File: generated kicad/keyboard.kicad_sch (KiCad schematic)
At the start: 190 parts

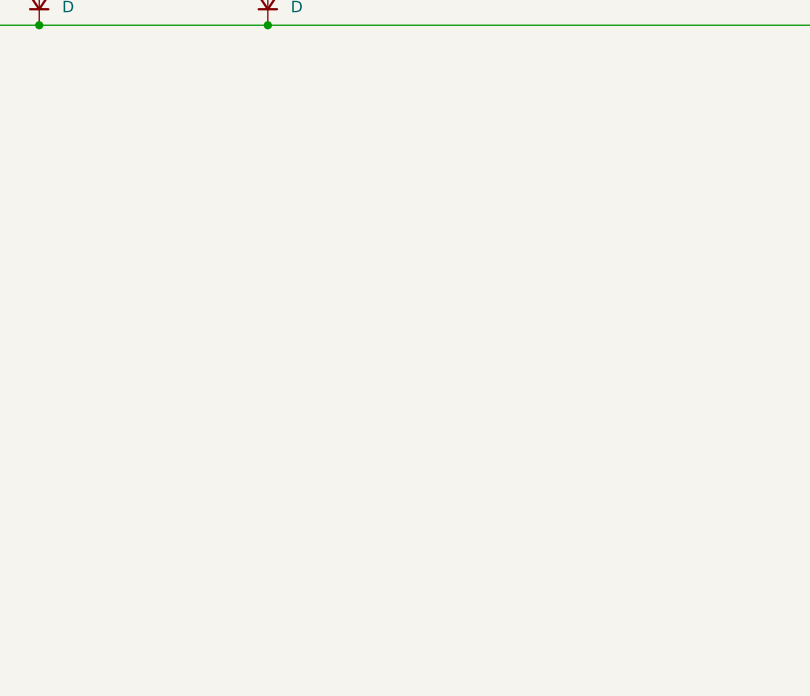
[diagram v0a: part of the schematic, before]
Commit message: blackpill footprint added
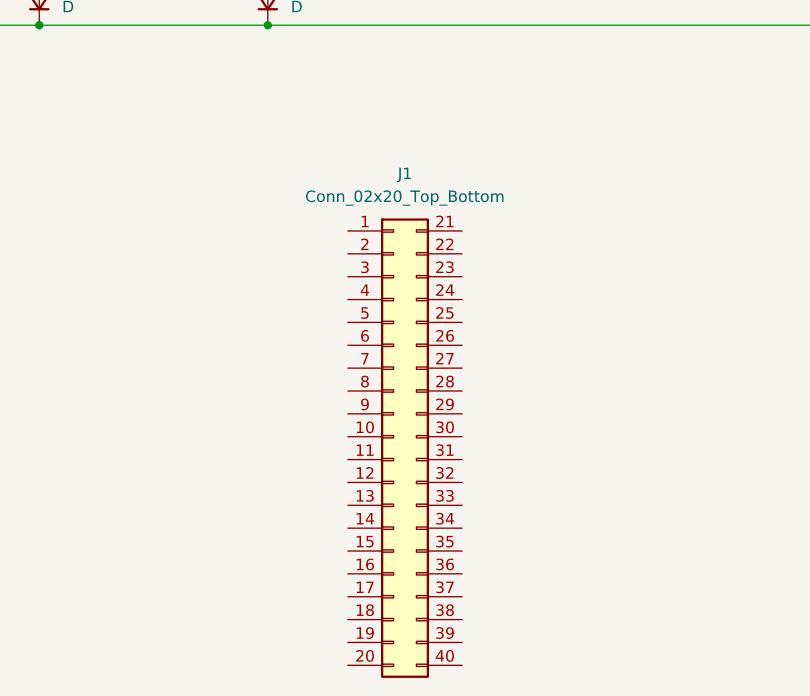
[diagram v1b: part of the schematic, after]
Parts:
- added J1: Conn_02x20_Top_Bottom, symbol Connector_Generic:Conn_02x20_Top_Bottom
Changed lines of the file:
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@@
+	)
+	(symbol
+		(lib_id "Connector_Generic:Conn_02x20_Top_Bottom")
+		(at 149.86 208.28 0)
+		(unit 1)
+		(exclude_from_sim no)
+		(in_bom yes)
+		(on_board yes)
+		(dnp no)
+		(fields_autoplaced yes)
+		(property "Reference" "J1"
+			(at 151.13 179.07 0)
+			(effects
+				(font
+					(size 1.27 1.27)
+				)
+			)
+		)
+		(property "Value" "Conn_02x20_Top_Bottom"
+			(at 151.13 181.61 0)
+			(effects
+				(font
+					(size 1.27 1.27)
+				)
+			)
+		)
+		(property "Footprint" ""
+			(at 149.86 208.28 0)
+			(effects
+				(font
+					(size 1.27 1.27)
+				)
+				(hide yes)
+			)
+		)
+		(property "Datasheet" "~"
+			(at 149.86 208.28 0)
+			(effects
+				(font
+					(size 1.27 1.27)
+				)
+				(hide yes)
+			)
+		)
+		(property "Description" "Generic connector, double row, 02x20, top/bottom pin numbering scheme (row 1: 1...pins_per_row, row2: pins_per_row+1 ... num_pins), script generated (kicad-library-utils/schlib/autogen/connector/)"
+			(at 149.86 208.28 0)
+			(effects
+				(font
+					(size 1.27 1.27)
+				)
+				(hide yes)
+			)
+		)
+		(pin "16"
+		)
+		(pin "10"
+		)
+		(pin "12"
+		)
+		(pin "20"
+		)
+		(pin "40"
+		)
+		(pin "9"
+		)
+		(pin "6"
+		)
+		(pin "7"
+		)
+		(pin "2"
+		)
+		(pin "5"
+		)
+		(pin "34"
+		)
+		(pin "37"
+		)
+		(pin "21"
+		)
+		(pin "17"
+		)
+		(pin "32"
+		)
+		(pin "14"
+		)
+		(pin "33"
+		)
+		(pin "39"
+		)
+		(pin "8"
+		)
+		(pin "13"
+		)
+		(pin "18"
+		)
+		(pin "25"
+		)
+		(pin "3"
+		)
+		(pin "36"
+		)
+		(pin "26"
+		)
+		(pin "31"
+		)
+		(pin "38"
+		)
+		(pin "1"
+		)
+		(pin "35"
+		)
+		(pin "19"
+		)
+		(pin "11"
+		)
+		(pin "24"
+		)
+		(pin "23"
+		)
+		(pin "28"
+		)
+		(pin "15"
+		)
+		(pin "22"
+		)
+		(pin "27"
+		)
+		(pin "29"
+		)
+		(pin "30"
+		)
+		(pin "4"
+		)
+		(instances
+			(project ""
+				(path "/4518914f-850f-4cd8-86f4-2792a0d788ad"
+					(reference "J1")
+					(unit 1)
+				)
+			)
+		)
 	)
 	(symbol

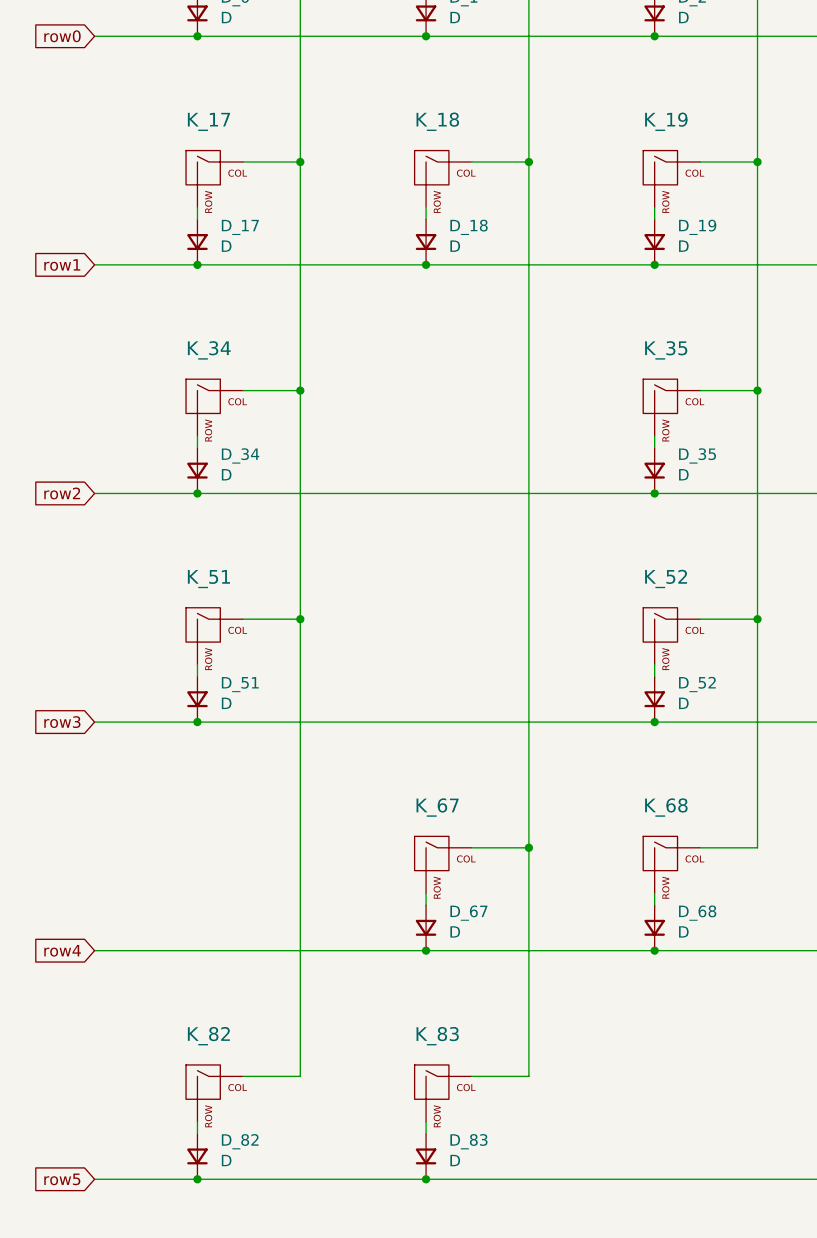
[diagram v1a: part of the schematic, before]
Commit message: wiring done, controller not placed
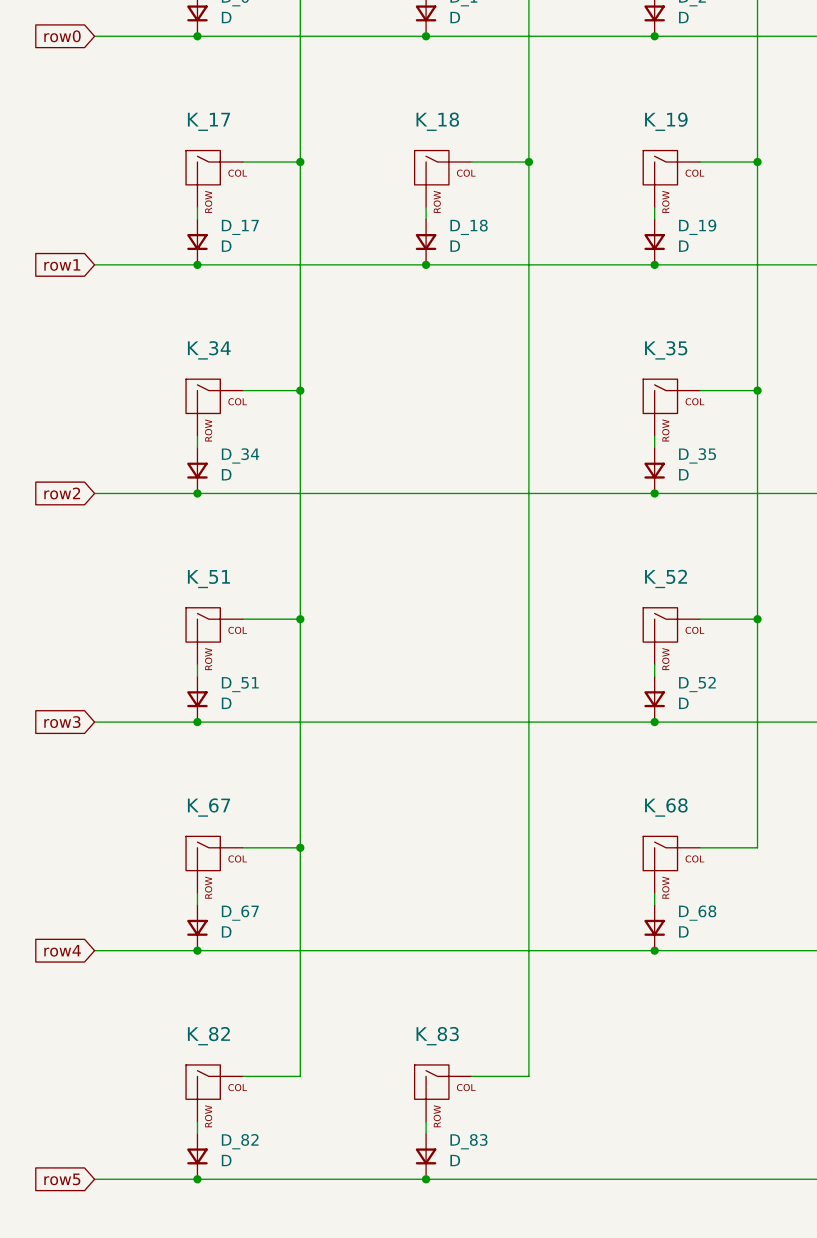
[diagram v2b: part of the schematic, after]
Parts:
- J1: footprint (none) -> my library:blackpill
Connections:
- net col0: now also K_67.1 (COL)
- net col1: no longer K_67.1 (COL)
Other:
- moved on the sheet: D_67, K_67
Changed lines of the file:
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@@
 	)
 	(junction
-		(at 71.12 125.73)
+		(at 45.72 125.73)
 		(diameter 0)
 		(color 0 0 0 0)
@@
 	)
 	(junction
-		(at 59.69 137.16)
+		(at 34.29 137.16)
 		(diameter 0)
 		(color 0 0 0 0)
@@
 	(wire
 		(pts
-			(xy 59.69 137.16) (xy 85.09 137.16)
-		)
-		(stroke
-			(width 0)
-			(type default)
-		)
-	)
-	(wire
-		(pts
 			(xy 212.09 162.56) (xy 313.69 162.56)
 		)
@@
 	(wire
 		(pts
-			(xy 71.12 151.13) (xy 71.12 125.73)
-		)
-		(stroke
-			(width 0)
-			(type default)
-		)
-	)
-	(wire
-		(pts
 			(xy 212.09 111.76) (xy 237.49 111.76)
 		)
@@
 	(wire
 		(pts
+			(xy 45.72 125.73) (xy 45.72 100.33)
+		)
+		(stroke
+			(width 0)
+			(type default)
+		)
+	)
+	(wire
+		(pts
 			(xy 471.17 49.53) (xy 477.52 49.53)
 		)
@@
 	(wire
 		(pts
+			(xy 34.29 137.16) (xy 85.09 137.16)
+		)
+		(stroke
+			(width 0)
+			(type default)
+		)
+	)
+	(wire
+		(pts
 			(xy 325.12 125.73) (xy 325.12 100.33)
 		)
@@
 	(wire
 		(pts
-			(xy 22.86 137.16) (xy 59.69 137.16)
+			(xy 22.86 137.16) (xy 34.29 137.16)
 		)
 		(stroke
@@
 	(wire
 		(pts
-			(xy 45.72 151.13) (xy 45.72 100.33)
+			(xy 45.72 151.13) (xy 45.72 125.73)
 		)
 		(stroke
@@
 	(wire
 		(pts
-			(xy 71.12 125.73) (xy 71.12 49.53)
+			(xy 71.12 49.53) (xy 71.12 151.13)
 		)
 		(stroke
@@
 	(wire
 		(pts
-			(xy 64.77 125.73) (xy 71.12 125.73)
+			(xy 39.37 125.73) (xy 45.72 125.73)
 		)
 		(stroke
@@
 	(wire
 		(pts
-			(xy 59.69 130.81) (xy 59.69 132.08)
+			(xy 34.29 130.81) (xy 34.29 132.08)
 		)
 		(stroke
@@
 	(symbol
 		(lib_id "MX_Alps_Hybrid:MX-NoLED")
-		(at 60.96 127 0)
+		(at 35.56 127 0)
 		(unit 1)
 		(exclude_from_sim no)
@@
 		(dnp no)
 		(property "Reference" "K_67"
-			(at 60.96 121.0818 0)
+			(at 35.56 121.0818 0)
 			(effects
 				(font
@@
 		)
 		(property "Value" "KEYSW"
-			(at 60.96 129.54 0)
+			(at 35.56 129.54 0)
 			(effects
 				(font
@@
 		)
 		(property "Footprint" "MX_Only:MXOnly-2.25U-Hotswap"
-			(at 60.96 127 0)
+			(at 35.56 127 0)
 			(effects
 				(font
@@
 		)
 		(property "Datasheet" ""
-			(at 60.96 127 0)
+			(at 35.56 127 0)
 			(effects
 				(font
@@
 		)
 		(property "Description" ""
-			(at 60.96 127 0)
+			(at 35.56 127 0)
 			(effects
 				(font
@@
 	(symbol
 		(lib_id "Device:D_Small")
-		(at 59.69 134.62 90)
+		(at 34.29 134.62 90)
 		(unit 1)
 		(exclude_from_sim no)
@@
 		(dnp no)
 		(property "Reference" "D_67"
-			(at 62.23 132.842 90)
+			(at 36.83 132.842 90)
 			(effects
 				(font
@@
 		)
 		(property "Value" "D"
-			(at 62.23 135.128 90)
+			(at 36.83 135.128 90)
 			(effects
 				(font
@@
 		)
 		(property "Footprint" "Diode_SMD:D_SOD-123"
-			(at 60.96 142.24 0)
+			(at 35.56 142.24 0)
 			(effects
 				(font
@@
 		)
 		(property "Datasheet" "~"
-			(at 60.96 142.24 0)
+			(at 35.56 142.24 0)
 			(effects
 				(font
@@
 		)
 		(property "Description" ""
-			(at 59.69 134.62 0)
+			(at 34.29 134.62 0)
 			(effects
 				(font
@@
 			)
 		)
-		(property "Footprint" ""
+		(property "Footprint" "my library:blackpill"
 			(at 149.86 208.28 0)
 			(effects

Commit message: pcb diodes and keys arranged
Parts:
- removed D_12, D_14, D_33, D_50, D_66, D_79, D_81: D, Diode_SMD:D_SOD-123, symbol Device:D_Small
- removed K_12, K_14, K_15, K_16, K_33, K_50, K_66, K_79, K_81: KEYSW, MX_Only:MXOnly-1U-Hotswap, symbol MX_Alps_Hybrid:MX-NoLED
- added D_17, D_18: D, Diode_SMD:D_SOD-123, symbol Device:D_Small
- added SW1, SW2: RotaryEncoder_Switch, Rotary_Encoder:RotaryEncoder_Alps_EC12E-Switch_Vertical_H20mm, symbol Device:RotaryEncoder_Switch
- renumbered D_0 to D_1, D_8 to D_10, D_9 to D_11, D_10 to D_12, D_11 to D_13, D_13 to D_14, D_17 to D_19, D_1 to D_2, D_18 to D_20, D_19 to D_21, D_20 to D_22, D_21 to D_23, D_22 to D_24, D_23 to D_25, D_24 to D_26, D_25 to D_27, D_26 to D_28, D_27 to D_29, D_2 to D_3, D_28 to D_30, D_29 to D_31, D_30 to D_32, D_31 to D_33, D_32 to D_34, D_34 to D_35, D_35 to D_36, D_36 to D_37, D_37 to D_38, D_38 to D_39, D_94 to D_4, D_39 to D_40, D_40 to D_41, D_41 to D_42, D_42 to D_43, D_43 to D_44, D_44 to D_45, D_45 to D_46, D_46 to D_47, D_47 to D_48, D_48 to D_49, D_3 to D_5, D_49 to D_50, D_4 to D_6, D_67 to D_66, D_68 to D_67, D_69 to D_68, D_70 to D_69, D_5 to D_7, D_71 to D_70, D_72 to D_71, D_73 to D_72, D_74 to D_73, D_75 to D_74, D_76 to D_75, D_77 to D_76, D_78 to D_77, D_80 to D_78, D_82 to D_79, D_6 to D_8, D_83 to D_80, D_84 to D_81, D_85 to D_82, D_86 to D_83, D_87 to D_84, D_88 to D_85, D_89 to D_86, D_90 to D_87, D_91 to D_88, D_92 to D_89, D_7 to D_9, D_93 to D_90, K_0 to K_1, K_8 to K_10, K_9 to K_11, K_10 to K_12, K_11 to K_13, K_13 to K_14, K_17 to K_15, K_18 to K_16, K_19 to K_17, K_20 to K_18, K_21 to K_19, K_1 to K_2, K_22 to K_20, K_23 to K_21, K_24 to K_22, K_25 to K_23, K_26 to K_24, K_27 to K_25, K_28 to K_26, K_29 to K_27, K_30 to K_28, K_31 to K_29, K_2 to K_3, K_32 to K_30, K_34 to K_31, K_35 to K_32, K_36 to K_33, K_37 to K_34, K_38 to K_35, K_39 to K_36, K_40 to K_37, K_41 to K_38, K_42 to K_39, K_94 to K_4, K_43 to K_40, K_44 to K_41, K_45 to K_42, K_46 to K_43, K_47 to K_44, K_48 to K_45, K_49 to K_46, K_51 to K_47, K_52 to K_48, K_53 to K_49, K_3 to K_5, K_54 to K_50, K_55 to K_51, K_56 to K_52, K_57 to K_53, K_58 to K_54, K_59 to K_55, K_60 to K_56, K_61 to K_57, K_62 to K_58, K_63 to K_59, K_4 to K_6, K_64 to K_60, K_65 to K_61, K_67 to K_62, K_68 to K_63, K_69 to K_64, K_70 to K_65, K_71 to K_66, K_72 to K_67, K_73 to K_68, K_74 to K_69, K_5 to K_7, K_75 to K_70, K_76 to K_71, K_77 to K_72, K_78 to K_73, K_80 to K_74, K_82 to K_75, K_83 to K_76, K_84 to K_77, K_85 to K_78, K_86 to K_79, K_6 to K_8, K_87 to K_80, K_88 to K_81, K_89 to K_82, K_90 to K_83, K_91 to K_84, K_92 to K_85, K_93 to K_86, K_7 to K_9
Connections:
- net row0 is gone; now on net col17: D_1.1 (K), D_10.1 (K), D_11.1 (K), D_12.1 (K), D_13.1 (K), D_14.1 (K), D_15.1 (K), D_16.1 (K), D_2.1 (K), D_3.1 (K), D_4.1 (K), D_5.1 (K), D_6.1 (K), D_7.1 (K), D_8.1 (K), D_9.1 (K)
- net col15: now also SW1.B; no longer K_29.1 (COL), K_45.1 (COL), K_60.1 (COL), K_84.1 (COL)
- net col16: now also SW1.A; no longer K_30.1 (COL), K_46.1 (COL), K_61.1 (COL), K_74.1 (COL), K_85.1 (COL)
- net col17: now also K_29.1 (COL), K_45.1 (COL), K_60.1 (COL), K_84.1 (COL), D_17.1 (K), D_18.1 (K), SW1.S1; no longer K_86.1 (COL)
- net at D_15.2 (A): now also SW1.C
- net at D_16.2 (A): now also SW1.S2
- net col13: no longer names the net of K_43.1 (COL), K_59.1 (COL), K_73.1 (COL), K_82.1 (COL)
- new net: D_17.2 (A), SW2.C
- new net: D_18.2 (A), SW2.S2
- new net col18: SW2.B
- new net col19: SW2.A
- new net col20: K_30.1 (COL), K_46.1 (COL), K_61.1 (COL), K_74.1 (COL), K_85.1 (COL), SW2.S1
- new net col21: K_86.1 (COL)

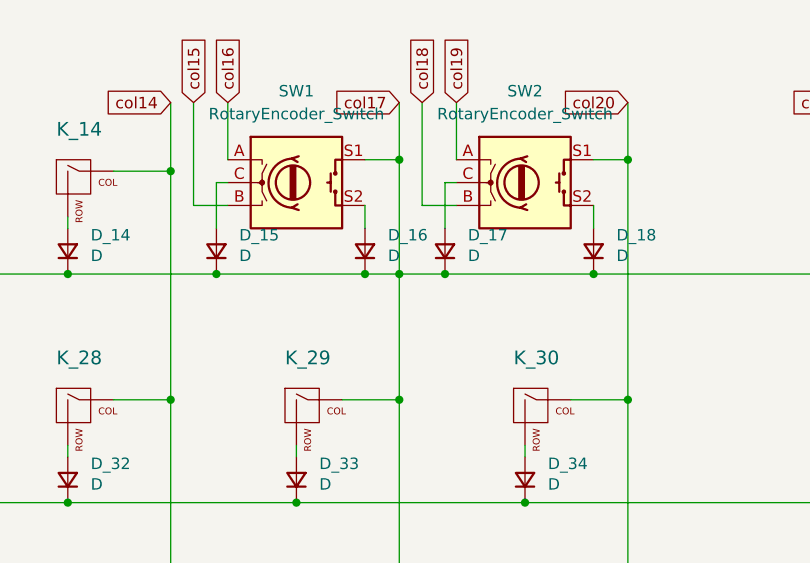
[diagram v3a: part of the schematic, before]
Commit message: routed tracks and fixed accidental intersection near R1
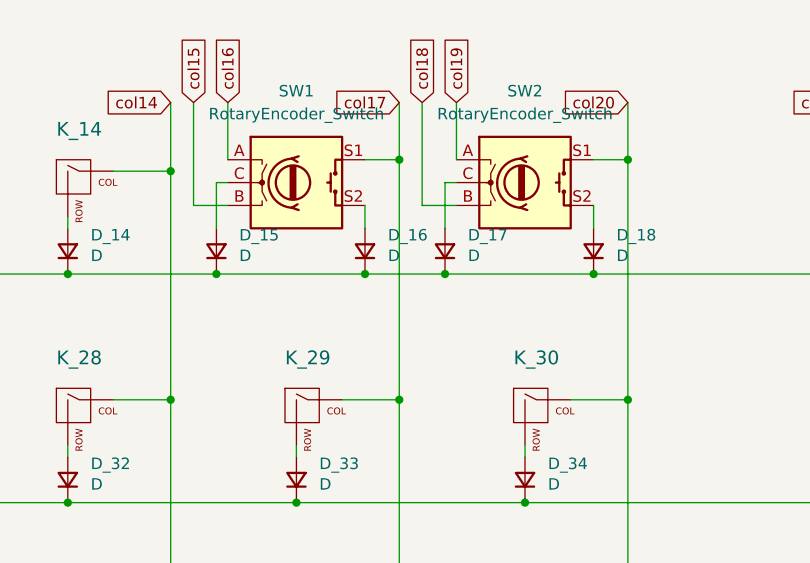
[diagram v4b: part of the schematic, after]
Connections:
- net col17: no longer D_1.1 (K), D_10.1 (K), D_11.1 (K), D_12.1 (K), D_13.1 (K), D_14.1 (K), D_15.1 (K), D_16.1 (K), D_17.1 (K), D_18.1 (K), D_2.1 (K), D_3.1 (K), D_4.1 (K), D_5.1 (K), D_6.1 (K), D_7.1 (K), D_8.1 (K), D_9.1 (K)
- new net row0: D_1.1 (K), D_10.1 (K), D_11.1 (K), D_12.1 (K), D_13.1 (K), D_14.1 (K), D_15.1 (K), D_16.1 (K), D_17.1 (K), D_18.1 (K), D_2.1 (K), D_3.1 (K), D_4.1 (K), D_5.1 (K), D_6.1 (K), D_7.1 (K), D_8.1 (K), D_9.1 (K)
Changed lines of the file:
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@@
-	)
-	(junction
-		(at 426.72 35.56)
-		(diameter 0)
-		(color 0 0 0 0)
 	)
 	(junction
@@
 	(wire
 		(pts
-			(xy 426.72 35.56) (xy 426.72 49.53)
-		)
-		(stroke
-			(width 0)
-			(type default)
-		)
-	)
-	(wire
-		(pts
 			(xy 90.17 100.33) (xy 96.52 100.33)
 		)
@@
 	(wire
 		(pts
-			(xy 426.72 35.56) (xy 431.8 35.56)
+			(xy 422.91 35.56) (xy 431.8 35.56)
 		)
 		(stroke
@@
 	(wire
 		(pts
-			(xy 422.91 35.56) (xy 426.72 35.56)
-		)
-		(stroke
-			(width 0)
-			(type default)
-		)
-	)
-	(wire
-		(pts
 			(xy 440.69 137.16) (xy 487.68 137.16)
 		)
@@
 	(wire
 		(pts
-			(xy 426.72 22.86) (xy 426.72 35.56)
-		)
-		(stroke
+			(xy 426.72 22.86) (xy 426.72 49.53)
+		)
+		(stroke
